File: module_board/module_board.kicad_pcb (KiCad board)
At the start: 2 copper layers, 22 x 42 mm, 129 parts, among them U1 CH32V003FxUx, U10 CH32V003FxUx, U11 CH32V003FxUx, U12 CH32V003FxUx, U13 CH32V003FxUx, U14 CH32V003FxUx, U15 CH32V003FxUx, U16 CH32V003FxUx, U2 CH32V003FxUx, U3 CH32V003FxUx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

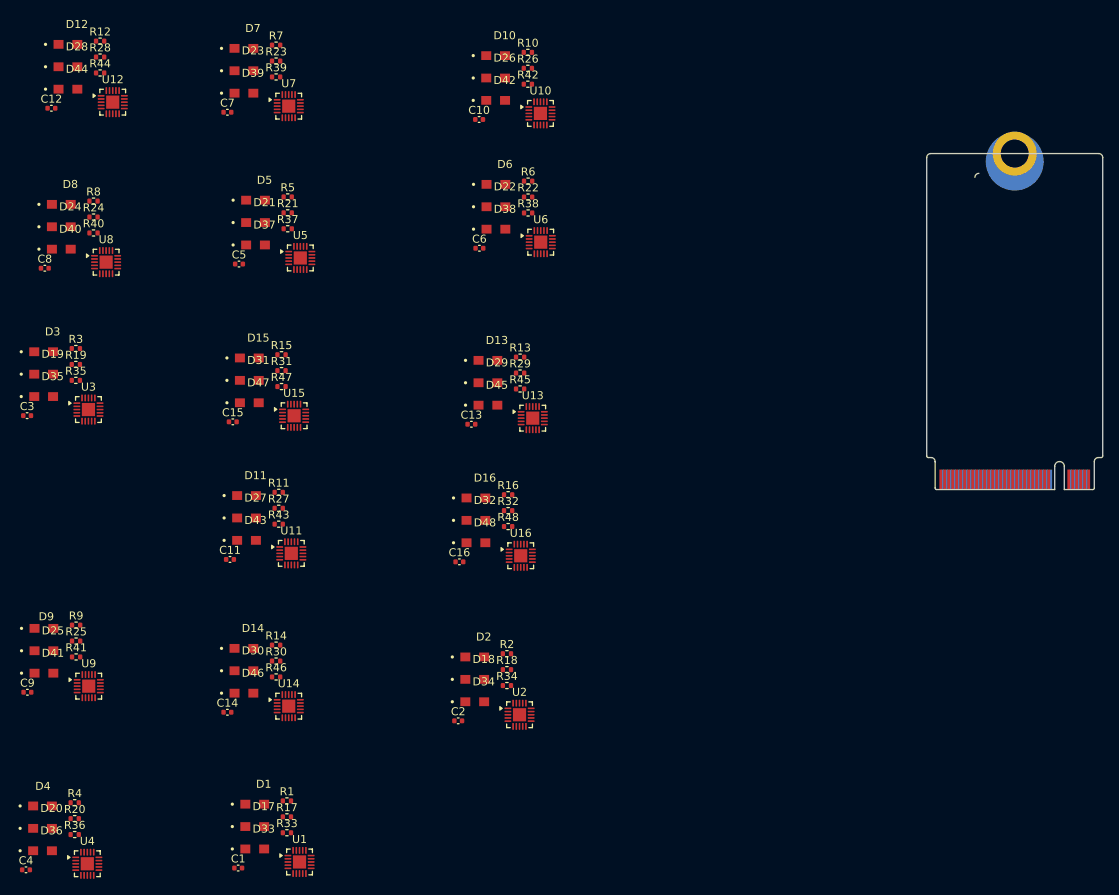
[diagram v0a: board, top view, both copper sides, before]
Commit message: ruined all the traces on MB
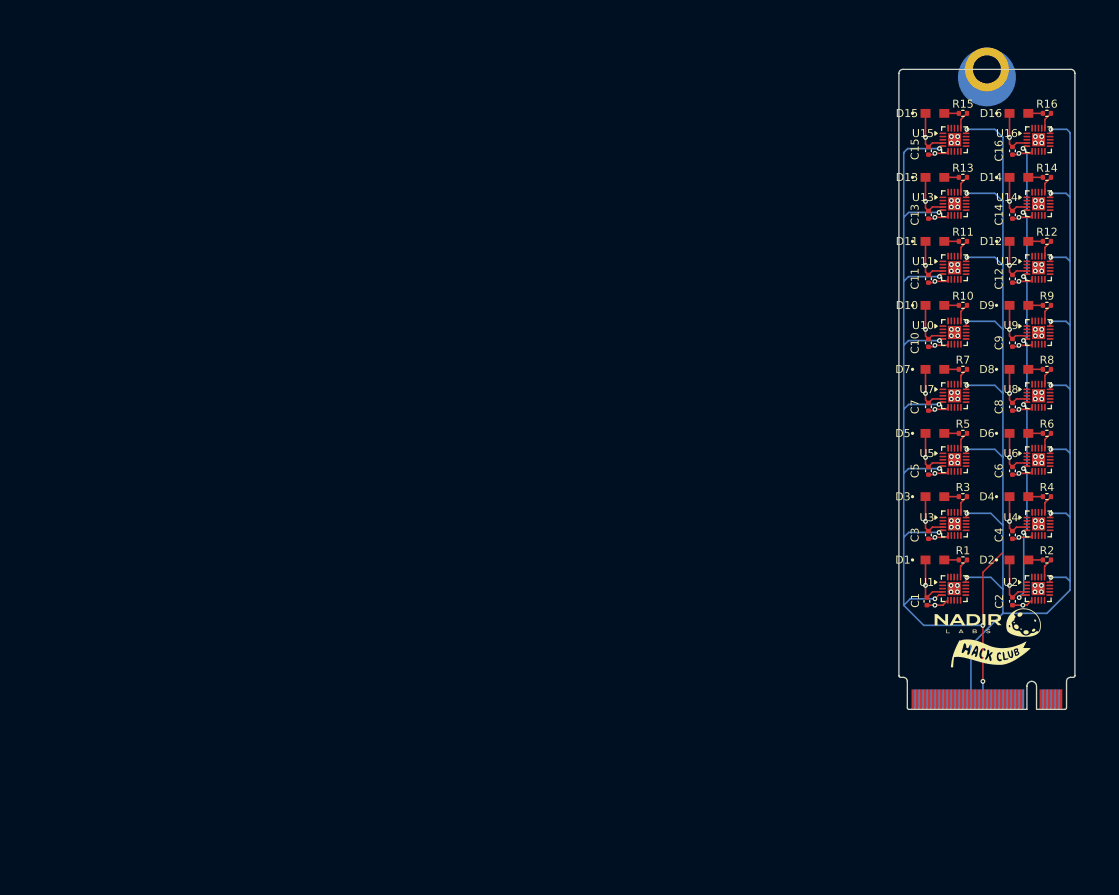
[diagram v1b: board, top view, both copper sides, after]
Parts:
- removed D17, D18, D19, D20, D21, D22, D23, D24, D25, D26, D27, D28, D29, D30, D31, D32: APT2012LVBC/D (BLUE), APT2012SGC:APT2012SGC
- removed D33, D34, D35, D36, D37, D38, D39, D40, D41, D42, D43, D44, D45, D46, D47, D48: APT2012EC (RED), APT2012SGC:APT2012SGC
- removed R17, R18, R19, R20, R21, R22, R23, R24, R25, R26, R27, R28, R29, R30, R31, R32: 220, Resistor_SMD:R_0402_1005Metric
- removed R33, R34, R35, R36, R37, R38, R39, R40, R41, R42, R43, R44, R45, R46, R47, R48: 170, Resistor_SMD:R_0402_1005Metric
- added G***: LOGO, asset_lib:nl_bw_large, F.Cu at (173.0, 123.5)
- added G***: LOGO, asset_lib:hc_bw_small, F.Cu at (173.5, 127.0)
- U$2: footprint m2bkey:m2bkey -> M.2-Templates:M.2-B-KEY
- moved C9 130.7 mm to (176.2, 88.2), turned to 90 degrees
- moved C4 130.2 mm to (176.2, 112.2), turned to 90 degrees
- moved D9 128.4 mm to (177.0, 83.5)
- moved D4 128.0 mm to (177.0, 107.4)
- moved R9 127.8 mm to (180.5, 83.5)
- moved R4 127.4 mm to (180.5, 107.4)
- moved U9 126.7 mm to (179.4, 86.9)
- moved U4 126.3 mm to (179.4, 110.8)
- moved C8 122.2 mm to (176.2, 96.2), turned to 90 degrees
- moved C12 122.0 mm to (176.2, 80.2), turned to 90 degrees
- moved D8 121.5 mm to (177.0, 91.5)
- moved D12 121.4 mm to (177.0, 75.5)
- moved R8 121.0 mm to (180.5, 91.5)
- moved R12 121.0 mm to (180.5, 75.5)
- moved U8 117.7 mm to (179.4, 94.8)
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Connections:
- U$2 pad P$40: (no net) -> MOD_SPI_CLK
- U$2 pad P$46: (no net) -> MOD_CS
- U$2 pad P$7: (no net) -> SWDIO
- U$2 pad P$9: (no net) -> SWDCLK
- U1 pad 18: Net-(U1-PD4) -> unconnected-(U1-PD4-Pad18)
- U1 pad 21: +3V3 -> GND
- U1 pad 4: +3V3 -> GND
- U1 pad 6: GND -> +3V3
- U1 pad 7: Net-(U1-PC0) -> unconnected-(U1-PC0-Pad7)
- U10 pad 18: Net-(U10-PD4) -> unconnected-(U10-PD4-Pad18)
- U10 pad 21: +3V3 -> GND
- U10 pad 4: +3V3 -> GND
- U10 pad 6: GND -> +3V3
- U10 pad 7: Net-(U10-PC0) -> unconnected-(U10-PC0-Pad7)
- U11 pad 18: Net-(U11-PD4) -> unconnected-(U11-PD4-Pad18)
- U11 pad 21: +3V3 -> GND
- U11 pad 4: +3V3 -> GND
- U11 pad 6: GND -> +3V3
- U11 pad 7: Net-(U11-PC0) -> unconnected-(U11-PC0-Pad7)
- U12 pad 18: Net-(U12-PD4) -> unconnected-(U12-PD4-Pad18)
- U12 pad 21: +3V3 -> GND
- U12 pad 4: +3V3 -> GND
- U12 pad 6: GND -> +3V3
- U12 pad 7: Net-(U12-PC0) -> unconnected-(U12-PC0-Pad7)
- U13 pad 18: Net-(U13-PD4) -> unconnected-(U13-PD4-Pad18)
- U13 pad 21: +3V3 -> GND
- U13 pad 4: +3V3 -> GND
- U13 pad 6: GND -> +3V3
- U13 pad 7: Net-(U13-PC0) -> unconnected-(U13-PC0-Pad7)
- U14 pad 18: Net-(U14-PD4) -> unconnected-(U14-PD4-Pad18)
- U14 pad 21: +3V3 -> GND
- U14 pad 4: +3V3 -> GND
- U14 pad 6: GND -> +3V3
- U14 pad 7: Net-(U14-PC0) -> unconnected-(U14-PC0-Pad7)
- U15 pad 18: Net-(U15-PD4) -> unconnected-(U15-PD4-Pad18)
- U15 pad 21: +3V3 -> GND
- U15 pad 4: +3V3 -> GND
- U15 pad 6: GND -> +3V3
- U15 pad 7: Net-(U15-PC0) -> unconnected-(U15-PC0-Pad7)
- U16 pad 18: Net-(U16-PD4) -> unconnected-(U16-PD4-Pad18)
- U16 pad 21: +3V3 -> GND
- U16 pad 4: +3V3 -> GND
- U16 pad 6: GND -> +3V3
- U16 pad 7: Net-(U16-PC0) -> unconnected-(U16-PC0-Pad7)
- U2 pad 18: Net-(U2-PD4) -> unconnected-(U2-PD4-Pad18)
- U2 pad 21: +3V3 -> GND
- U2 pad 4: +3V3 -> GND
- U2 pad 6: GND -> +3V3
- U2 pad 7: Net-(U2-PC0) -> unconnected-(U2-PC0-Pad7)
- U3 pad 18: Net-(U3-PD4) -> unconnected-(U3-PD4-Pad18)
- U3 pad 21: +3V3 -> GND
- U3 pad 4: +3V3 -> GND
- U3 pad 6: GND -> +3V3
- U3 pad 7: Net-(U3-PC0) -> unconnected-(U3-PC0-Pad7)
- U4 pad 18: Net-(U4-PD4) -> unconnected-(U4-PD4-Pad18)
- U4 pad 21: +3V3 -> GND
- U4 pad 4: +3V3 -> GND
- U4 pad 6: GND -> +3V3
- U4 pad 7: Net-(U4-PC0) -> unconnected-(U4-PC0-Pad7)
- U5 pad 18: Net-(U5-PD4) -> unconnected-(U5-PD4-Pad18)
- U5 pad 21: +3V3 -> GND
- U5 pad 4: +3V3 -> GND
- U5 pad 6: GND -> +3V3
- U5 pad 7: Net-(U5-PC0) -> unconnected-(U5-PC0-Pad7)
- U6 pad 18: Net-(U6-PD4) -> unconnected-(U6-PD4-Pad18)
- U6 pad 21: +3V3 -> GND
- U6 pad 4: +3V3 -> GND
- U6 pad 6: GND -> +3V3
- U6 pad 7: Net-(U6-PC0) -> unconnected-(U6-PC0-Pad7)
- U7 pad 18: Net-(U7-PD4) -> unconnected-(U7-PD4-Pad18)
- U7 pad 21: +3V3 -> GND
- U7 pad 4: +3V3 -> GND
- U7 pad 6: GND -> +3V3
- U7 pad 7: Net-(U7-PC0) -> unconnected-(U7-PC0-Pad7)
- U8 pad 18: Net-(U8-PD4) -> unconnected-(U8-PD4-Pad18)
- U8 pad 21: +3V3 -> GND
- U8 pad 4: +3V3 -> GND
- U8 pad 6: GND -> +3V3
- U8 pad 7: Net-(U8-PC0) -> unconnected-(U8-PC0-Pad7)
- U9 pad 18: Net-(U9-PD4) -> unconnected-(U9-PD4-Pad18)
- U9 pad 21: +3V3 -> GND
- U9 pad 4: +3V3 -> GND
- U9 pad 6: GND -> +3V3
- U9 pad 7: Net-(U9-PC0) -> unconnected-(U9-PC0-Pad7)
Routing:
- net MOD_CS: track 0.00 -> 208.4 mm, vias 0 -> 16
- net MOD_SPI_CLK: track 0.00 -> 192.6 mm, vias 0 -> 18
- net GND: track 0.00 -> 103.2 mm, vias 0 -> 80
- net +3V3: track 0.00 -> 42.2 mm, vias 0 -> 16
- net Net-(U2-PD2): track 0.00 -> 2.47 mm
- net Net-(U1-PD2): track 0.00 -> 2.47 mm
- net Net-(U4-PD2): track 0.00 -> 2.27 mm
- net Net-(U3-PD2): track 0.00 -> 2.27 mm
- net Net-(U9-PD2): track 0.00 -> 2.26 mm
- net Net-(U10-PD2): track 0.00 -> 2.26 mm
- net Net-(U16-PD2): track 0.00 -> 2.16 mm
- net Net-(U15-PD2): track 0.00 -> 2.16 mm
- net Net-(U8-PD2): track 0.00 -> 2.16 mm
- net Net-(U7-PD2): track 0.00 -> 2.16 mm
- net Net-(U6-PD2): track 0.00 -> 2.16 mm
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- added copper zone on In1.Cu, net +3V3
- added copper zone on In2.Cu, net GND
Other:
- board size 22 x 42 mm -> 22 x 80 mm
- copper layers 2 -> 4
